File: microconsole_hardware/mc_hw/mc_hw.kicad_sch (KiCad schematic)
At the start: 10 parts

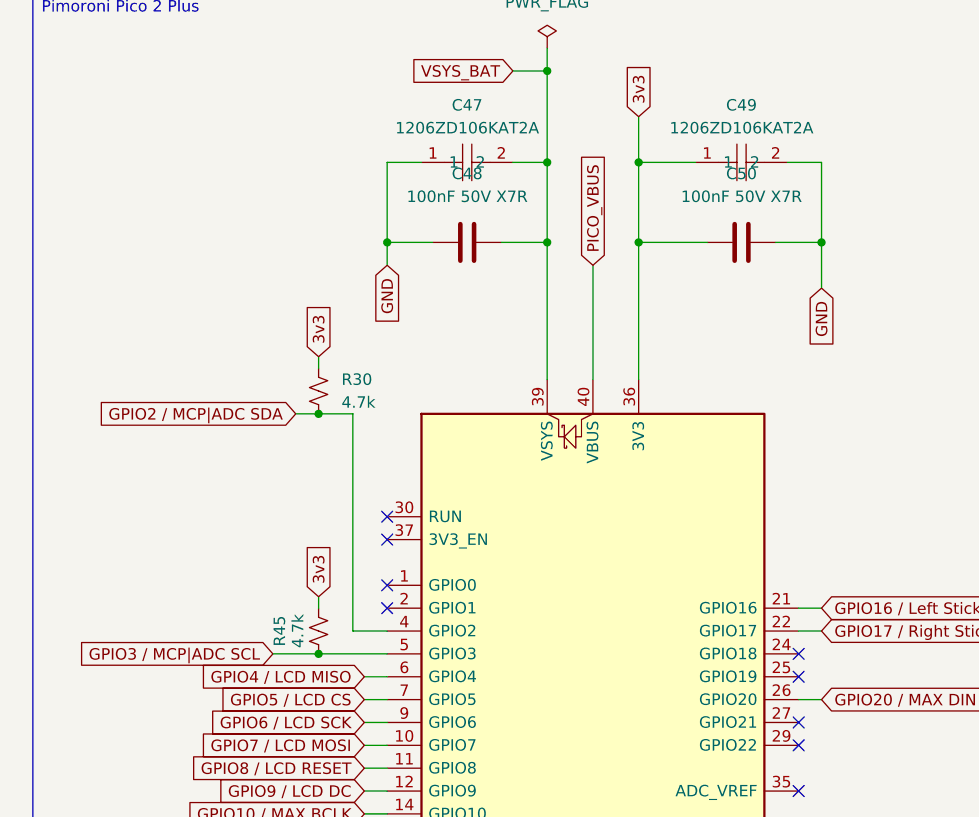
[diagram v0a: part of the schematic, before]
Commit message: resistor and capacitor consolidation.
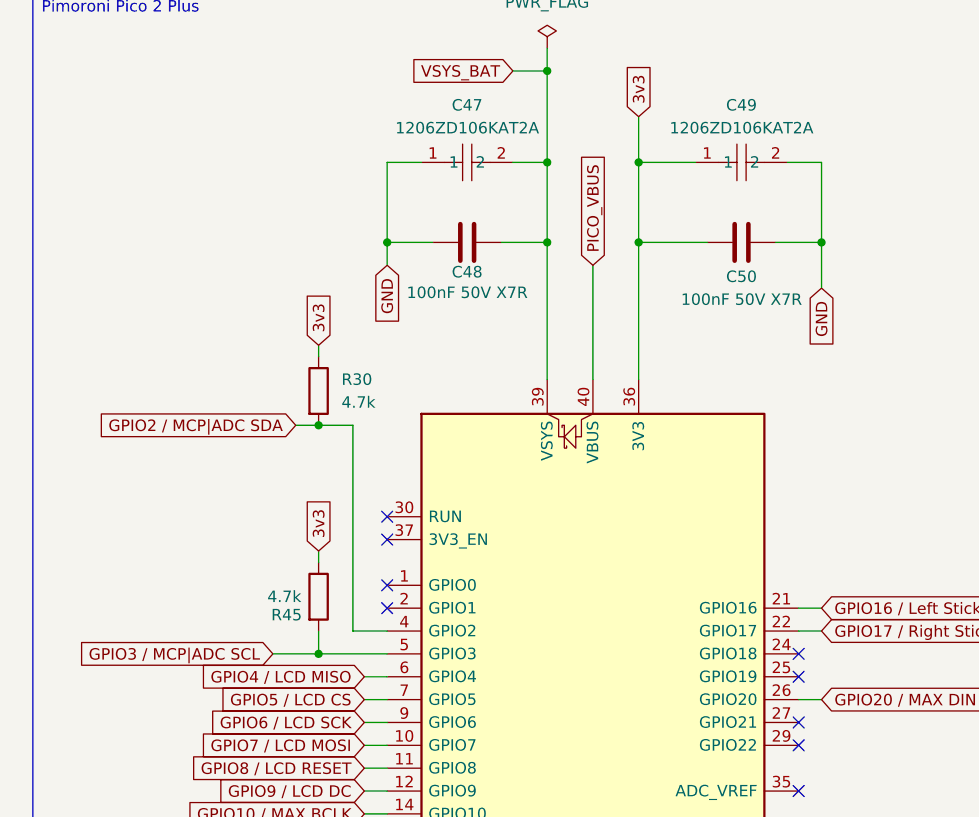
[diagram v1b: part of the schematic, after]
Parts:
- R30, R45: footprint PCM_SparkFun-Resistor:R_0603_1608Metric -> Resistor_SMD:R_0603_1608Metric; symbol PCM_SparkFun-Resistor:0.47_0603 -> Device:R
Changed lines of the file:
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@@
+	)
+	(junction
+		(at 173.99 109.22)
+		(diameter 0)
+		(color 0 0 0 0)
+	)
+	(junction
+		(at 173.99 83.82)
+		(diameter 0)
+		(color 0 0 0 0)
 	)
 	(junction
@@
 	)
 	(junction
-		(at 173.99 109.22)
-		(diameter 0)
-		(color 0 0 0 0)
-	)
-	(junction
-		(at 173.99 82.55)
-		(diameter 0)
-		(color 0 0 0 0)
-	)
-	(junction
 		(at 199.39 44.45)
 		(diameter 0)
@@
 	(wire
 		(pts
-			(xy 173.99 76.2) (xy 173.99 77.47)
+			(xy 173.99 74.93) (xy 173.99 76.2)
 		)
 		(stroke
@@
 	(wire
 		(pts
-			(xy 177.8 106.68) (xy 177.8 82.55)
+			(xy 177.8 106.68) (xy 177.8 83.82)
 		)
 		(stroke
@@
 	(wire
 		(pts
+			(xy 173.99 97.79) (xy 173.99 99.06)
+		)
+		(stroke
+			(width 0)
+			(type default)
+		)
+	)
+	(wire
+		(pts
+			(xy 173.99 106.68) (xy 173.99 109.22)
+		)
+		(stroke
+			(width 0)
+			(type default)
+		)
+	)
+	(wire
+		(pts
 			(xy 215.9 54.61) (xy 209.55 54.61)
 		)
@@
 	(wire
 		(pts
-			(xy 171.45 82.55) (xy 173.99 82.55)
+			(xy 171.45 83.82) (xy 177.8 83.82)
 		)
 		(stroke
@@
 	(wire
 		(pts
-			(xy 168.91 109.22) (xy 181.61 109.22)
-		)
-		(stroke
-			(width 0)
-			(type default)
-		)
-	)
-	(wire
-		(pts
-			(xy 177.8 82.55) (xy 173.99 82.55)
+			(xy 168.91 109.22) (xy 173.99 109.22)
 		)
 		(stroke
@@
 	(wire
 		(pts
-			(xy 173.99 102.87) (xy 173.99 104.14)
-		)
-		(stroke
-			(width 0)
-			(type default)
-		)
-	)
-	(wire
-		(pts
 			(xy 194.31 227.33) (xy 194.31 215.9)
 		)
@@
 		)
 	)
+	(wire
+		(pts
+			(xy 173.99 109.22) (xy 181.61 109.22)
+		)
+		(stroke
+			(width 0)
+			(type default)
+		)
+	)
 	(global_label "GPIO6 {slash} LCD SCK"
 		(shape input)
@@
 	(global_label "3v3"
 		(shape input)
-		(at 173.99 76.2 90)
+		(at 173.99 74.93 90)
 		(fields_autoplaced yes)
 		(effects
@@
 		)
 		(property "Intersheetrefs" "${INTERSHEET_REFS}"
-			(at 173.99 50.8991 90)
+			(at 173.99 49.6291 90)
 			(hide yes)
 			(show_name no)
@@
 	(global_label "GPIO2 {slash} MCP|ADC SDA"
 		(shape input)
-		(at 171.45 82.55 180)
+		(at 171.45 83.82 180)
 		(fields_autoplaced yes)
 		(effects
@@
 		)
 		(property "Intersheetrefs" "${INTERSHEET_REFS}"
-			(at 171.45 82.55 0)
+			(at 171.45 83.82 0)
 			(hide yes)
 			(show_name no)
@@
 	(global_label "3v3"
 		(shape input)
-		(at 173.99 102.87 90)
+		(at 173.99 97.79 90)
 		(fields_autoplaced yes)
 		(effects
@@
 		)
 		(property "Intersheetrefs" "${INTERSHEET_REFS}"
-			(at 173.99 77.3877 90)
+			(at 173.99 72.3077 90)
 			(hide yes)
 			(show_name no)
@@
 	)
 	(symbol
-		(lib_id "PCM_SparkFun-Resistor:0.47_0603")
-		(at 173.99 80.01 270)
+		(lib_id "Device:R")
+		(at 173.99 80.01 0)
 		(unit 1)
 		(body_style 1)
@@
 		(fields_autoplaced yes)
 		(property "Reference" "R30"
-			(at 176.53 78.7399 90)
+			(at 176.53 78.7399 0)
 			(show_name no)
 			(do_not_autoplace no)
@@
 		)
 		(property "Value" "4.7k"
-			(at 176.53 81.2799 90)
+			(at 176.53 81.2799 0)
 			(show_name no)
 			(do_not_autoplace no)
@@
 			)
 		)
-		(property "Footprint" "PCM_SparkFun-Resistor:R_0603_1608Metric"
-			(at 169.418 80.01 0)
+		(property "Footprint" "Resistor_SMD:R_0603_1608Metric"
+			(at 172.212 80.01 90)
 			(hide yes)
 			(show_name no)
@@
 		)
 		(property "Datasheet" "https://industrial.panasonic.com/cdbs/www-data/pdf/RDN0000/AOA0000C313.pdf"
-			(at 165.1 80.01 0)
+			(at 173.99 80.01 0)
 			(hide yes)
 			(show_name no)
@@
 		)
 		(property "Description" "Resistor"
-			(at 162.56 80.01 0)
+			(at 173.99 80.01 0)
 			(hide yes)
 			(show_name no)
@@
 		)
 		(property "PROD_ID" "RES-20715"
-			(at 167.132 80.01 0)
+			(at 173.99 86.868 0)
 			(hide yes)
 			(show_name no)
@@
 		(in_pos_files yes)
 		(dnp no)
-		(fields_autoplaced yes)
 		(property "Reference" "C50"
-			(at 220.98 55.88 90)
+			(at 220.98 67.31 90)
 			(show_name no)
 			(do_not_autoplace no)
@@
 		)
 		(property "Value" "100nF 50V X7R"
-			(at 220.98 58.42 90)
+			(at 220.98 69.85 90)
 			(show_name no)
 			(do_not_autoplace no)
@@
 	)
 	(symbol
-		(lib_id "PCM_SparkFun-Resistor:0.47_0603")
-		(at 173.99 106.68 270)
+		(lib_id "Device:R")
+		(at 173.99 102.87 0)
 		(unit 1)
 		(body_style 1)
@@
 		(dnp no)
 		(property "Reference" "R45"
-			(at 169.672 106.68 0)
+			(at 170.434 104.902 0)
 			(show_name no)
 			(do_not_autoplace no)
@@
 		)
 		(property "Value" "4.7k"
-			(at 171.704 106.68 0)
-			(show_name no)
-			(do_not_autoplace no)
-			(effects
-				(font
-					(size 1.27 1.27)
-				)
-			)
-		)
-		(property "Footprint" "PCM_SparkFun-Resistor:R_0603_1608Metric"
-			(at 169.418 106.68 0)
+			(at 170.18 102.87 0)
+			(show_name no)
+			(do_not_autoplace no)
+			(effects
+				(font
+					(size 1.27 1.27)
+				)
+			)
+		)
+		(property "Footprint" "Resistor_SMD:R_0603_1608Metric"
+			(at 172.212 102.87 90)
 			(hide yes)
 			(show_name no)
@@
 		)
 		(property "Datasheet" "https://industrial.panasonic.com/cdbs/www-data/pdf/RDN0000/AOA0000C313.pdf"
-			(at 165.1 106.68 0)
+			(at 173.99 102.87 0)
 			(hide yes)
 			(show_name no)
@@
 		)
 		(property "Description" "Resistor"
-			(at 162.56 106.68 0)
+			(at 173.99 102.87 0)
 			(hide yes)
 			(show_name no)
@@
 		)
 		(property "PROD_ID" "RES-20715"
-			(at 167.132 106.68 0)
+			(at 173.99 109.728 0)
 			(hide yes)
 			(show_name no)
@@
 		(in_pos_files yes)
 		(dnp no)
-		(fields_autoplaced yes)
 		(property "Reference" "C48"
-			(at 190.5 55.88 90)
+			(at 190.5 66.802 90)
 			(show_name no)
 			(do_not_autoplace no)
@@
 		)
 		(property "Value" "100nF 50V X7R"
-			(at 190.5 58.42 90)
-			(show_name no)
-			(do_not_autoplace no)
+			(at 190.5 69.088 90)
+			(show_name no)
+			(do_not_autoplace no)

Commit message: finish cleanup of footprints
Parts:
- A2: value RaspberryPi_Pico -> Pimoroni Pico Plus 2; footprint Module:RaspberryPi_Pico_Common_Unspecified -> project_parts:RaspberryPi_Pico_Common_Unspecified
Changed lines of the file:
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@@
 			)
 		)
-		(property "Value" "RaspberryPi_Pico"
+		(property "Value" "Pimoroni Pico Plus 2"
 			(at 206.6133 153.67 0)
 			(show_name no)
@@
 			)
 		)
-		(property "Footprint" "Module:RaspberryPi_Pico_Common_Unspecified"
+		(property "Footprint" "project_parts:RaspberryPi_Pico_Common_Unspecified"
 			(at 204.47 163.83 0)
 			(hide yes)

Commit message: consolidate parts 1
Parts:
- R30, R45: MPN (none) -> RC0603FR-074K7L; Manufacturer (none) -> YAGEO; Power (none) -> 0.1W; Tolerance (none) -> 1%
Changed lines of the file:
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@@
+			)
+		)
+		(property "Power" ""
+			(at 204.47 116.84 0)
+			(hide yes)
+			(show_name no)
+			(do_not_autoplace no)
+			(effects
+				(font
+					(size 1.27 1.27)
+				)
 			)
 		)
@@
 			)
 		)
-		(property "Datasheet" "https://industrial.panasonic.com/cdbs/www-data/pdf/RDN0000/AOA0000C313.pdf"
+		(property "Datasheet" ""
 			(at 173.99 80.01 0)
 			(hide yes)
@@
 		(property "PROD_ID" "RES-20715"
 			(at 173.99 86.868 0)
+			(hide yes)
+			(show_name no)
+			(do_not_autoplace no)
+			(effects
+				(font
+					(size 1.27 1.27)
+				)
+			)
+		)
+		(property "MPN" "RC0603FR-074K7L"
+			(at 173.99 80.01 0)
+			(hide yes)
+			(show_name no)
+			(do_not_autoplace no)
+			(effects
+				(font
+					(size 1.27 1.27)
+				)
+			)
+		)
+		(property "Manufacturer" "YAGEO"
+			(at 173.99 80.01 0)
+			(hide yes)
+			(show_name no)
+			(do_not_autoplace no)
+			(effects
+				(font
+					(size 1.27 1.27)
+				)
+			)
+		)
+		(property "Power" "0.1W"
+			(at 173.99 80.01 0)
+			(hide yes)
+			(show_name no)
+			(do_not_autoplace no)
+			(effects
+				(font
+					(size 1.27 1.27)
+				)
+			)
+		)
+		(property "Tolerance" "1%"
+			(at 173.99 80.01 0)
 			(hide yes)
 			(show_name no)
@@
 			)
 		)
+		(property "Power" ""
+			(at 220.98 63.5 90)
+			(hide yes)
+			(show_name no)
+			(do_not_autoplace no)
+			(effects
+				(font
+					(size 1.27 1.27)
+				)
+			)
+		)
 		(pin "1"
 		)
@@
 			)
 		)
+		(property "Power" ""
+			(at 179.07 222.25 0)
+			(hide yes)
+			(show_name no)
+			(do_not_autoplace no)
+			(effects
+				(font
+					(size 1.27 1.27)
+				)
+			)
+		)
 		(pin "1"
 		)
@@
 			)
 		)
-		(property "Datasheet" "https://industrial.panasonic.com/cdbs/www-data/pdf/RDN0000/AOA0000C313.pdf"
+		(property "Datasheet" ""
 			(at 173.99 102.87 0)
 			(hide yes)
@@
 		(property "PROD_ID" "RES-20715"
 			(at 173.99 109.728 0)
+			(hide yes)
+			(show_name no)
+			(do_not_autoplace no)
+			(effects
+				(font
+					(size 1.27 1.27)
+				)
+			)
+		)
+		(property "MPN" "RC0603FR-074K7L"
+			(at 173.99 102.87 0)
+			(hide yes)
+			(show_name no)
+			(do_not_autoplace no)
+			(effects
+				(font
+					(size 1.27 1.27)
+				)
+			)
+		)
+		(property "Manufacturer" "YAGEO"
+			(at 173.99 102.87 0)
+			(hide yes)
+			(show_name no)
+			(do_not_autoplace no)
+			(effects
+				(font
+					(size 1.27 1.27)
+				)
+			)
+		)
+		(property "Power" "0.1W"
+			(at 173.99 102.87 0)
+			(hide yes)
+			(show_name no)
+			(do_not_autoplace no)
+			(effects
+				(font
+					(size 1.27 1.27)
+				)
+			)
+		)
+		(property "Tolerance" "1%"
+			(at 173.99 102.87 0)
 			(hide yes)
 			(show_name no)
@@
 			)
 		)
+		(property "Power" ""
+			(at 215.9 243.84 0)
+			(hide yes)
+			(show_name no)
+			(do_not_autoplace no)
+			(effects
+				(font
+					(size 1.27 1.27)
+				)
+			)
+		)
 		(pin "1"
 		)
@@
 			)
 		)
+		(property "Power" ""
+			(at 220.98 54.61 0)
+			(hide yes)
+			(show_name no)
+			(do_not_autoplace no)
+			(effects
+				(font
+					(size 1.27 1.27)
+				)
+			)
+		)
 		(pin "1"
 		)
@@
 			)
 		)
+		(property "Power" ""
+			(at 173.99 220.98 90)
+			(hide yes)
+			(show_name no)
+			(do_not_autoplace no)
+			(effects
+				(font
+					(size 1.27 1.27)
+				)
+			)
+		)
 		(pin "1"
 		)
@@
 		(property "Manufacturer" "KEMET"
 			(at 190.5 63.5 0)
+			(hide yes)
+			(show_name no)
+			(do_not_autoplace no)
+			(effects
+				(font
+					(size 1.27 1.27)
+				)
+			)
+		)
+		(property "Power" ""
+			(at 190.5 63.5 90)
 			(hide yes)
 			(show_name no)
@@
 			(hide yes)
 			(show_name no)
+			(do_not_autoplace no)
+			(effects
+				(font
+					(size 1.27 1.27)
+				)
+			)
+		)
+		(property "Power" ""
+			(at 190.5 54.61 0)
+			(hide yes)
+			(show_name no)

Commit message: bom cleanup
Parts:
- C45, C47, C49: Tolerance (none) -> 10%; Voltage (none) -> 10V
- C46, C48, C50: Tolerance (none) -> 10%; Voltage (none) -> 50V
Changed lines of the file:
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@@
+			)
+		)
+		(property "Tolerance" "10%"
+			(at 220.98 63.5 90)
+			(hide yes)
+			(show_name no)
+			(do_not_autoplace no)
+			(effects
+				(font
+					(size 1.27 1.27)
+				)
+			)
+		)
+		(property "Voltage" "50V"
+			(at 220.98 63.5 90)
+			(hide yes)
+			(show_name no)
+			(do_not_autoplace no)
+			(effects
+				(font
+					(size 1.27 1.27)
+				)
 			)
 		)
@@
 		)
 		(property "Power" ""
+			(at 179.07 222.25 0)
+			(hide yes)
+			(show_name no)
+			(do_not_autoplace no)
+			(effects
+				(font
+					(size 1.27 1.27)
+				)
+			)
+		)
+		(property "Tolerance" "10%"
+			(at 179.07 222.25 0)
+			(hide yes)
+			(show_name no)
+			(do_not_autoplace no)
+			(effects
+				(font
+					(size 1.27 1.27)
+				)
+			)
+		)
+		(property "Voltage" "50V"
 			(at 179.07 222.25 0)
 			(hide yes)
@@
 			)
 		)
-		(property "Datasheet" "https://lcsc.com/product-detail/presales_AVX-1206ZD106KAT2A_C597553.html"
+		(property "Datasheet" ""
 			(at 220.98 64.77 0)
 			(hide yes)
@@
 		)
 		(property "Power" ""
+			(at 220.98 54.61 0)
+			(hide yes)
+			(show_name no)
+			(do_not_autoplace no)
+			(effects
+				(font
+					(size 1.27 1.27)
+				)
+			)
+		)
+		(property "Tolerance" "10%"
+			(at 220.98 54.61 0)
+			(hide yes)
+			(show_name no)
+			(do_not_autoplace no)
+			(effects
+				(font
+					(size 1.27 1.27)
+				)
+			)
+		)
+		(property "Voltage" "10V"
 			(at 220.98 54.61 0)
 			(hide yes)
@@
 			)
 		)
-		(property "Datasheet" "https://lcsc.com/product-detail/presales_AVX-1206ZD106KAT2A_C597553.html"
+		(property "Datasheet" ""
 			(at 184.15 220.98 0)
 			(hide yes)
@@
 		)
 		(property "Power" ""
+			(at 173.99 220.98 90)
+			(hide yes)
+			(show_name no)
+			(do_not_autoplace no)
+			(effects
+				(font
+					(size 1.27 1.27)
+				)
+			)
+		)
+		(property "Tolerance" "10%"
+			(at 173.99 220.98 90)
+			(hide yes)
+			(show_name no)
+			(do_not_autoplace no)
+			(effects
+				(font
+					(size 1.27 1.27)
+				)
+			)
+		)
+		(property "Voltage" "10V"
 			(at 173.99 220.98 90)
 			(hide yes)
@@
 		)
 		(property "Power" ""
+			(at 190.5 63.5 90)
+			(hide yes)
+			(show_name no)
+			(do_not_autoplace no)
+			(effects
+				(font
+					(size 1.27 1.27)
+				)
+			)
+		)
+		(property "Tolerance" "10%"
+			(at 190.5 63.5 90)
+			(hide yes)
+			(show_name no)
+			(do_not_autoplace no)
+			(effects
+				(font
+					(size 1.27 1.27)
+				)
+			)
+		)
+		(property "Voltage" "50V"
 			(at 190.5 63.5 90)
 			(hide yes)
@@
 			)
 		)
-		(property "Datasheet" "https://lcsc.com/product-detail/presales_AVX-1206ZD106KAT2A_C597553.html"
+		(property "Datasheet" ""
 			(at 190.5 64.77 0)
 			(hide yes)
@@
 			(at 190.5 54.61 0)
 			(hide yes)
+			(show_name no)
+			(do_not_autoplace no)
+			(effects
+				(font
+					(size 1.27 1.27)
+				)
+			)
+		)
+		(property "Tolerance" "10%"
+			(at 190.5 54.61 0)
+			(hide yes)
+			(show_name no)
+			(do_not_autoplace no)
+			(effects
+				(font
+					(size 1.27 1.27)
+				)
+			)
+		)
+		(property "Voltage" "10V"
+			(at 190.5 54.61 0)
+			(hide yes)

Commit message: bom3
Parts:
- A2: MPN (none) -> PIM724; Manufacturer (none) -> Pimoroni
- DS1: MPN (none) -> MSP4021; Manufacturer (none) -> LCDWIKI
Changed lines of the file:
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@@
 			)
 		)
-		(property "Datasheet" "https://datasheets.raspberrypi.com/pico/pico-datasheet.pdf"
+		(property "Datasheet" "https://shop.pimoroni.com/products/pimoroni-pico-plus-2"
 			(at 204.47 166.37 0)
 			(hide yes)
@@
 		)
 		(property "Power" ""
+			(at 204.47 116.84 0)
+			(hide yes)
+			(show_name no)
+			(do_not_autoplace no)
+			(effects
+				(font
+					(size 1.27 1.27)
+				)
+			)
+		)
+		(property "MPN" "PIM724"
+			(at 204.47 116.84 0)
+			(hide yes)
+			(show_name no)
+			(do_not_autoplace no)
+			(effects
+				(font
+					(size 1.27 1.27)
+				)
+			)
+		)
+		(property "Manufacturer" "Pimoroni"
 			(at 204.47 116.84 0)
 			(hide yes)
@@
 			(at 215.9 243.84 0)
 			(hide yes)
+			(show_name no)
+			(do_not_autoplace no)
+			(effects
+				(font
+					(size 1.27 1.27)
+				)
+			)
+		)
+		(property "MPN" "MSP4021"
+			(at 215.9 243.84 0)
+			(hide yes)
+			(show_name no)
+			(do_not_autoplace no)
+			(effects
+				(font
+					(size 1.27 1.27)
+				)
+			)
+		)
+		(property "Manufacturer" "LCDWIKI"
+			(at 215.9 243.84 0)
+			(hide yes)

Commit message: dnp
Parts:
- A2, DS1: now not fitted
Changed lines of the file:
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@@
 		(on_board yes)
 		(in_pos_files yes)
-		(dnp no)
+		(dnp yes)
 		(fields_autoplaced yes)
 		(property "Reference" "A2"
@@
 		(on_board yes)
 		(in_pos_files yes)
-		(dnp no)
+		(dnp yes)
 		(fields_autoplaced yes)
 		(property "Reference" "DS1"
